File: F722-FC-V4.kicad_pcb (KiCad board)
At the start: 4 copper layers, 37.1 x 37.2 mm, 126 parts, among them J1 Conn_01x02, J10 Conn_01x08, J11 Conn_01x03, J12 Conn_01x02, J13 USB_B_Micro, J14 Conn_01x04, J15 Conn_01x04, J16 Conn_01x01, J17 Conn_01x04, J2 Conn_01x04, J3 Conn_01x04, J4 Conn_01x03, J5 Conn_01x03, J6 Conn_01x06, J7 Conn_01x06, J8 Conn_01x04, J9 Conn_01x08, Q1 BSS138, SW1 SW_Push, U1 LP2985-3.3, U10 W25Q128JVS, U2 STM32F722RETx, U3 LP2985-3.3, U4 MP4560_QFN10, U5 MP4560_QFN10, U6 MAX7456EUI+, U7 MPU-6000, U9 BMP388, Y1 27MHz

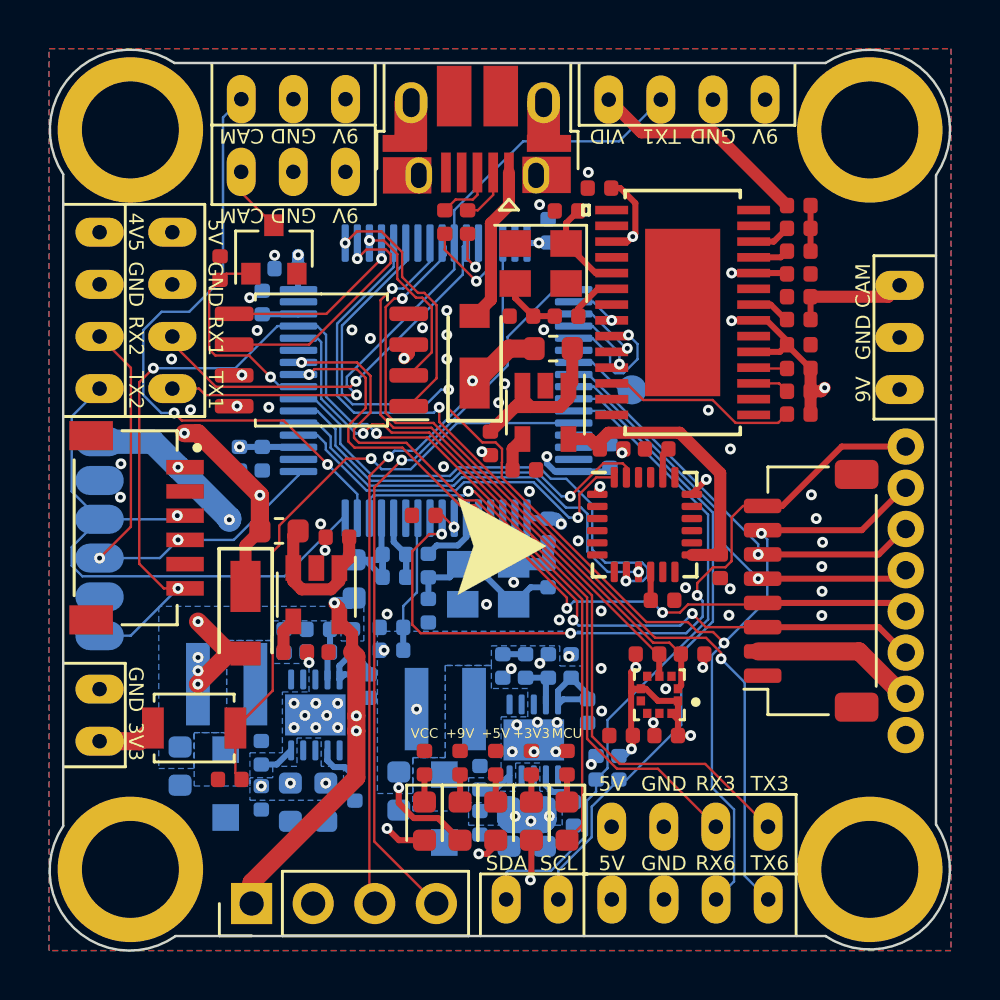
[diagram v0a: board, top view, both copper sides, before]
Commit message: Updated the schematics to include pictures
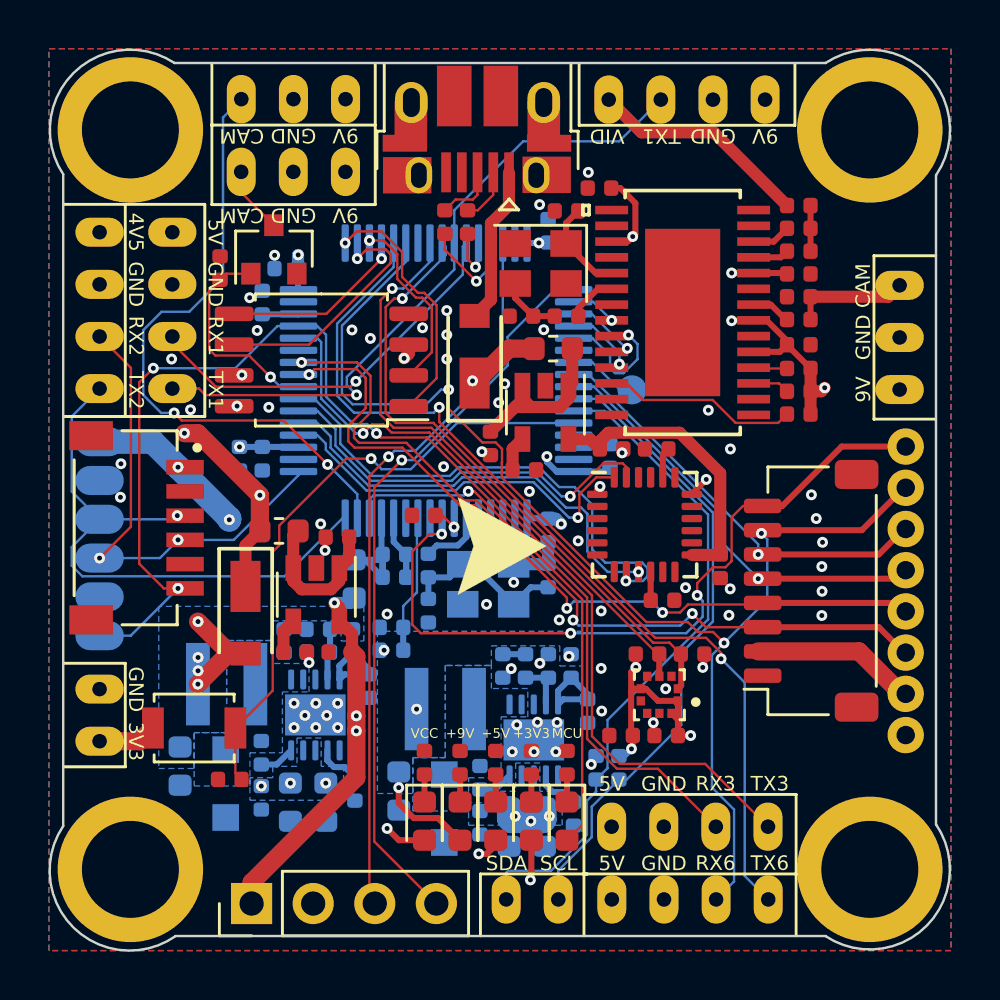
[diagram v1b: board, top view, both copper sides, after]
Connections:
- net /MCU/USB_D+ renamed /Connectors/USB_D+
- net /MCU/USB_D- renamed /Connectors/USB_D-

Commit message: Rerouted a bit
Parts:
- moved L4 13.8 mm to (105.6, 83.2)
- moved L3 6.19 mm to (106.3, 92.3)
- moved R1 4.44 mm to (89.4, 82.0)
- moved SW1 0.40 mm to (84.3, 100.9)
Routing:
- net VCC: track 50.0 -> 54.3 mm
- net /MCU/BUZ-_MCU: track 8.75 -> 11.8 mm
- net +3V3: track 53.8 -> 56.0 mm, vias 21 -> 23
- net /MCU/SPI3_CS: track 1.88 -> 3.72 mm
- net /Flash/SPI2_CS: track 10.5 -> 12.2 mm
- net /Flash/SPI2_MISO: track 7.52 -> 9.07 mm
- net /Connectors/M1: track 33.5 -> 34.9 mm
- net /Connectors/UART2_RX: track 20.0 -> 21.2 mm
- net /Connectors/UART3_RX: track 52.1 -> 51.2 mm
- net /Connectors/M4: track 17.4 -> 18.2 mm
- net +5V: track 66.8 -> 67.5 mm
- net /Flash/SPI2_SCK: track 9.82 -> 10.5 mm
- net +9V: track 65.0 -> 64.4 mm, vias 5 -> 7
- net /Connectors/M3: track 17.7 -> 18.3 mm
- net GND: vias 65 -> 67
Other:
- board text added: "CLK"
- board text added: "DIO"
- board text added: "MIDN WOLFE"
- board text added: "SWD"

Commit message: Changed around routing
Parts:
- removed C27, C30: 2.2uF, Capacitor_SMD:C_0603_1608Metric
- C24, C29: value 2.2uF -> 4.7uF
- C33, C34: value 560pF -> 390pF
- C36: value 2pF -> 1pF
- C46: value 2.2uF -> 2.2nF
- L1, L2: footprint Inductor_SMD:L_XGL4030 -> Inductor_SMD:L_Bourns-SRN3015
- R22: value 120k -> 165k
- R24: value 68k -> 93.1k
- moved C28 1.01 mm to (96.6, 104.5)
- moved C31 1.01 mm to (87.6, 103.4)
- moved C1 1.00 mm to (89.8, 92.0), turned to 0 degrees
- moved C16 1.00 mm to (89.9, 96.8)
- moved C2 1.00 mm to (88.0, 96.8)
- moved D1 1.00 mm to (86.0, 95.2)
- moved FB1 1.00 mm to (87.4, 91.8)
- moved J5 1.00 mm to (113.0, 83.8)
- moved U1 1.00 mm to (88.9, 94.4)
- moved C29 0.94 mm to (88.8, 104.0)
- moved R19 0.52 mm to (90.0, 103.4)
- moved C24 0.52 mm to (97.8, 105.0)
- moved R17 0.52 mm to (99.0, 104.5)
- moved L3 0.45 mm to (106.0, 91.9)
- moved L2 0.31 mm to (85.3, 99.4), turned to 90 degrees
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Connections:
- J10 pad 1: /Connectors/CURR -> VCC
- J10 pad 2: /Connectors/UART6_RX -> GND
- J10 pad 3: /Connectors/M4 -> /Connectors/CURR
- J10 pad 4: /Connectors/M3 -> /Connectors/UART6_RX
- J10 pad 5: /Connectors/M2 -> /Connectors/M1
- J10 pad 6: /Connectors/M1 -> /Connectors/M2
- J10 pad 7: VCC -> /Connectors/M3
- J10 pad 8: GND -> /Connectors/M4
- J9 pad 1: GND -> VCC
- J9 pad 2: VCC -> GND
- J9 pad 3: /Connectors/M1 -> /Connectors/CURR
- J9 pad 4: /Connectors/M2 -> /Connectors/UART6_RX
- J9 pad 5: /Connectors/M3 -> /Connectors/M1
- J9 pad 6: /Connectors/M4 -> /Connectors/M2
- J9 pad 7: /Connectors/UART6_RX -> /Connectors/M3
- J9 pad 8: /Connectors/CURR -> /Connectors/M4
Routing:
- net +3V3: track 56.0 -> 66.1 mm, vias 23 -> 27
- net /Connectors/CURR: track 30.3 -> 21.6 mm
- net /Connectors/UART2_TX: track 24.8 -> 20.4 mm, vias 1 -> 3
- net VCC: track 54.3 -> 50.8 mm, vias 8 -> 7
- net GND: track 4.03 -> 1.23 mm, vias 67 -> 69
- net Net-(C1-Pad1): track 6.31 -> 4.36 mm
- net /CAM: track 4.81 -> 6.69 mm
- net /Connectors/UART6_RX: track 53.0 -> 52.0 mm, vias 3 -> 2
- net +9V: track 64.4 -> 65.3 mm
- net /Connectors/LED: track 26.1 -> 26.9 mm
- net /Connectors/M4: track 18.2 -> 17.4 mm
- net +5V: track 67.5 -> 68.3 mm
- net /Connectors/M3: track 18.3 -> 17.6 mm
- net 4V5: track 32.8 -> 32.1 mm
- net /Connectors/M2: track 32.4 -> 33.1 mm
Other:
- board text added: "SWO"

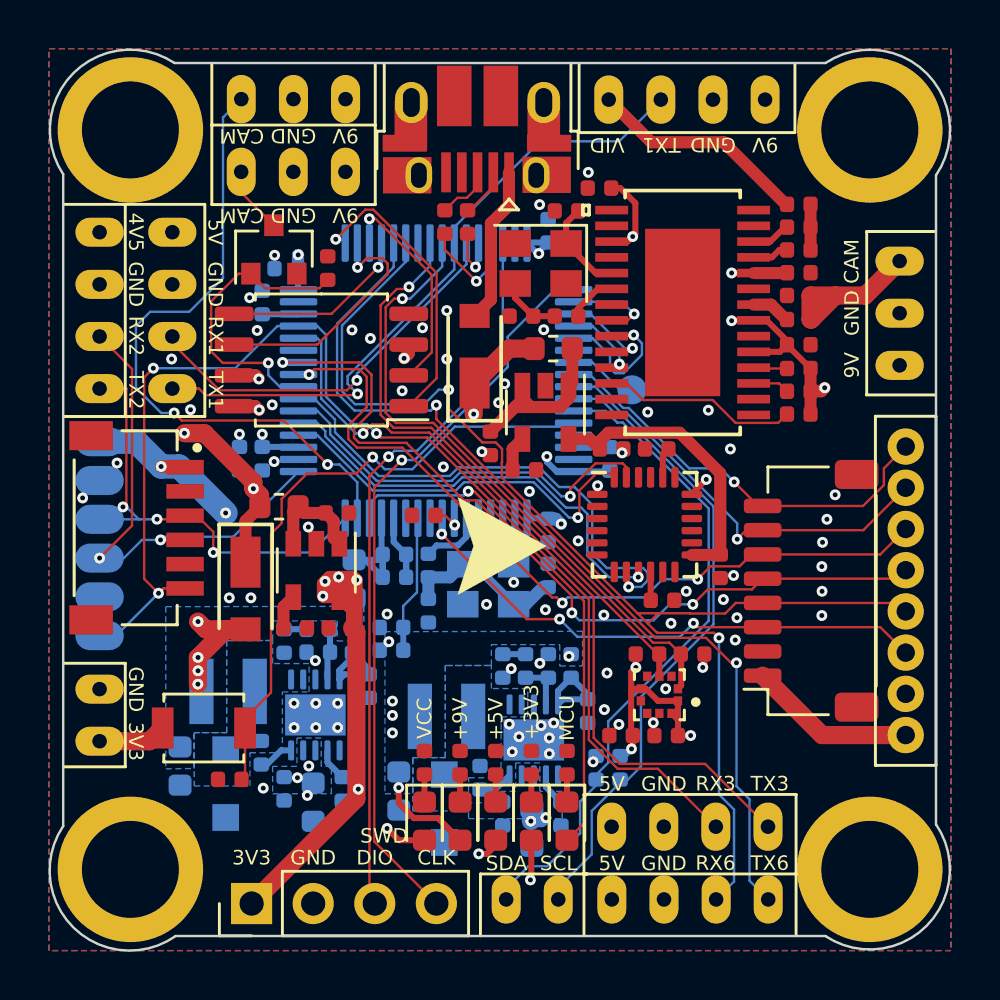
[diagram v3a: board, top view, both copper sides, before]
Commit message: Added teardrops
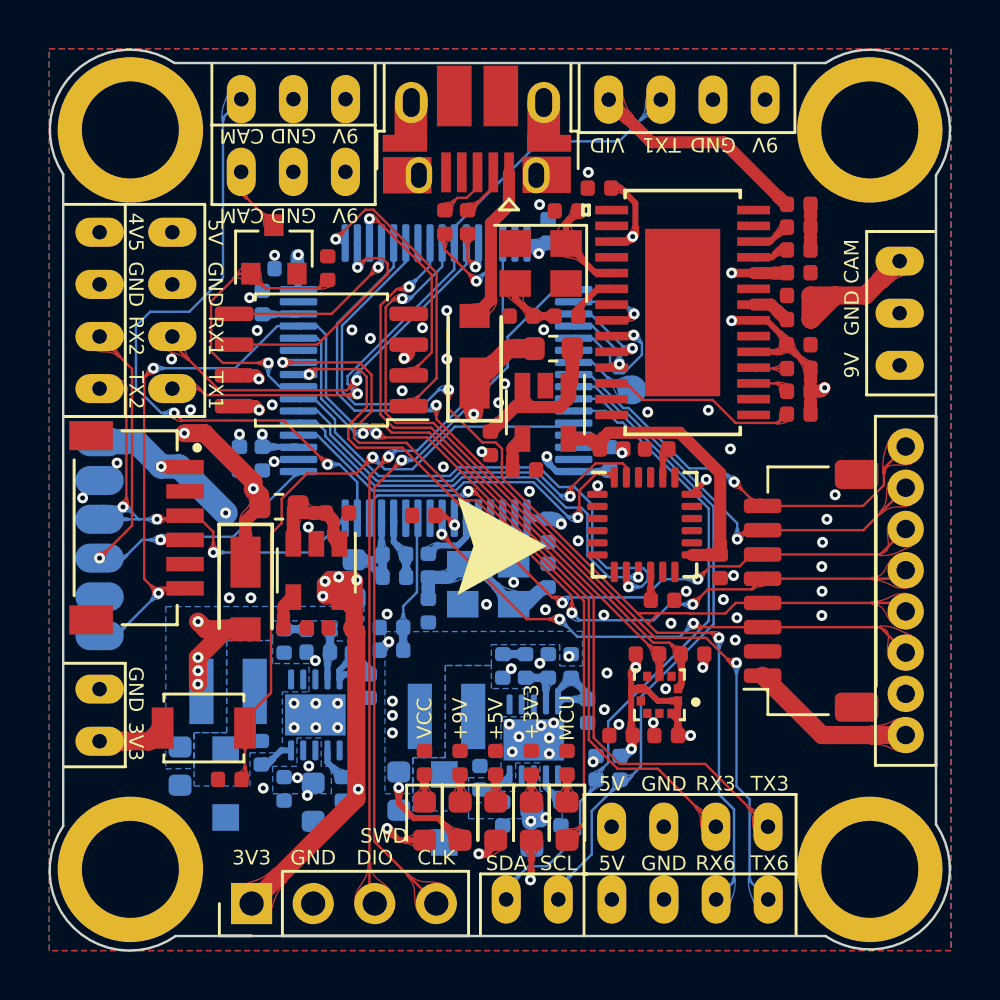
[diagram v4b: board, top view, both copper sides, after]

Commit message: Unknown changes
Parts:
- moved R15 1.35 mm to (93.8, 81.3)
- moved R7 1.35 mm to (94.8, 81.3)
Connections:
- net Net-(R15-Pad2) renamed /MCU/D-
- net Net-(R7-Pad2) renamed /MCU/D+
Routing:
- net /Connectors/USB_D-: track 2.05 -> 3.46 mm
- net /Connectors/USB_D+: track 2.35 -> 3.58 mm
- net /MCU/D+: track 2.55 -> 1.80 mm
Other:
- net class Test removed
- net class USB Data added: clearance 0.1, trace_width 0.1, via_dia 0.45, via_drill 0.2
